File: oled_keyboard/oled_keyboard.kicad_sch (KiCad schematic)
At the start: 116 parts, among them J1 Conn_01x20_Socket, J10 Conn_01x20_Socket, J11 Conn_01x20_Socket, J12 Conn_01x20_Socket, J2 Conn_01x20_Socket, J3 Conn_01x20_Socket, J4 Conn_01x20_Socket, J5 Conn_01x20_Socket, J6 Conn_01x20_Socket, J7 Conn_01x20_Socket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

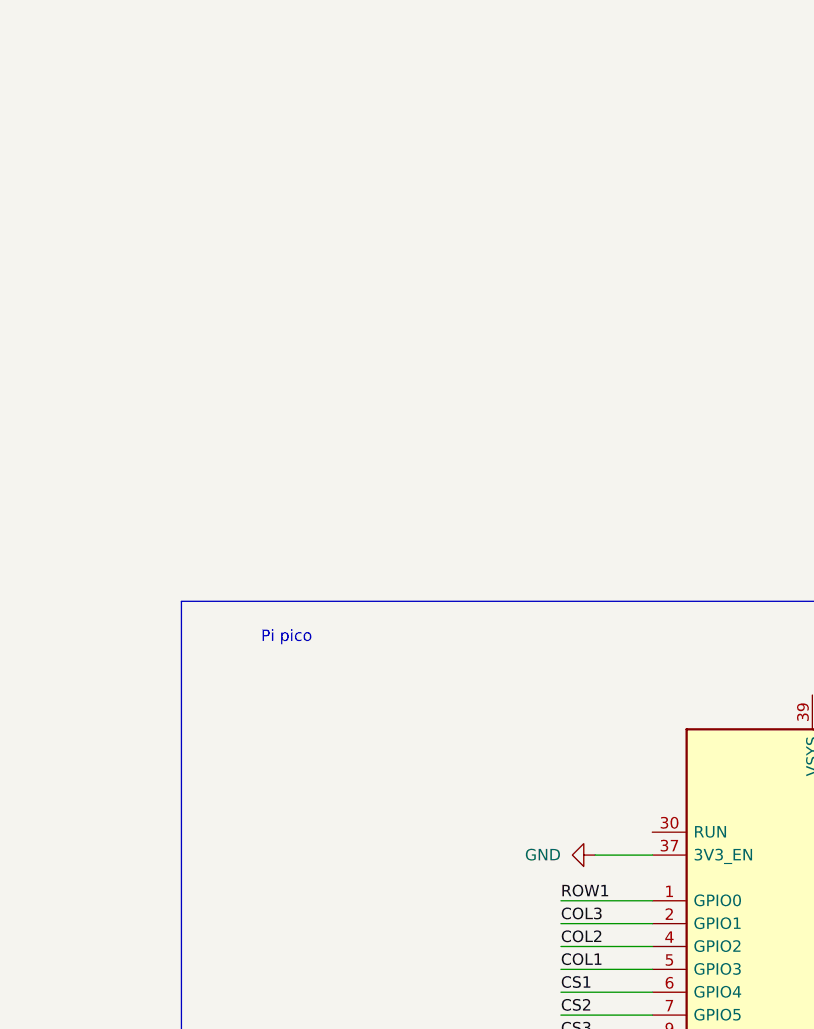
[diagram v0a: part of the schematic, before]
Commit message: fix: fixed reversed 20pin connector pinout
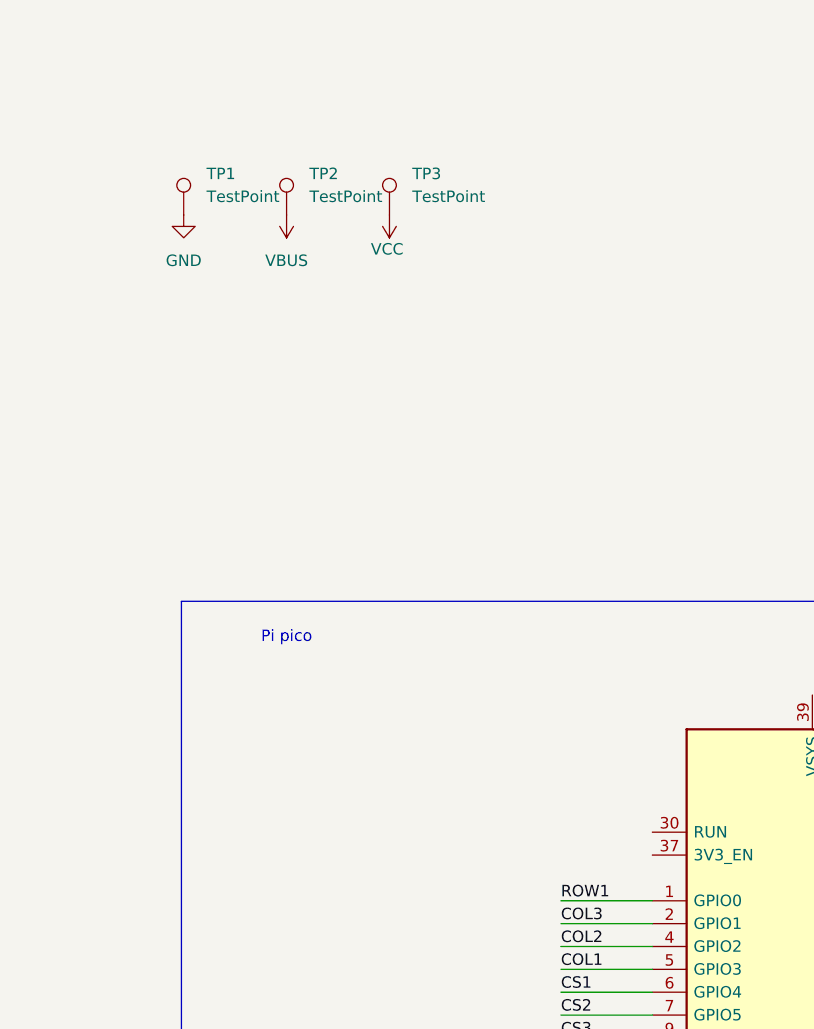
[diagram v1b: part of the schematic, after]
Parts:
- added TP1, TP2, TP3: TestPoint, TestPoint:TestPoint_Pad_3.0x3.0mm, symbol Connector:TestPoint
- J1, J10, J11, J12, J2, J3, J4, J5, J6, J7, J8, J9: footprint 20p_connector:HRS_TF31-20S-0.5SH_800_ -> Library:HRS_TF31-20S-0.5SH_800
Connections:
- net GND: now also TP1.1; no longer A1.37 (3V3_EN)
- net VBUS: now also TP2.1
- net VCC: now also TP3.1
